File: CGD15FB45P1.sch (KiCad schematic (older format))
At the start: 9 parts, among them J12 CONN_02X13, U6 74LVC8T245, U7 74LVC2G04

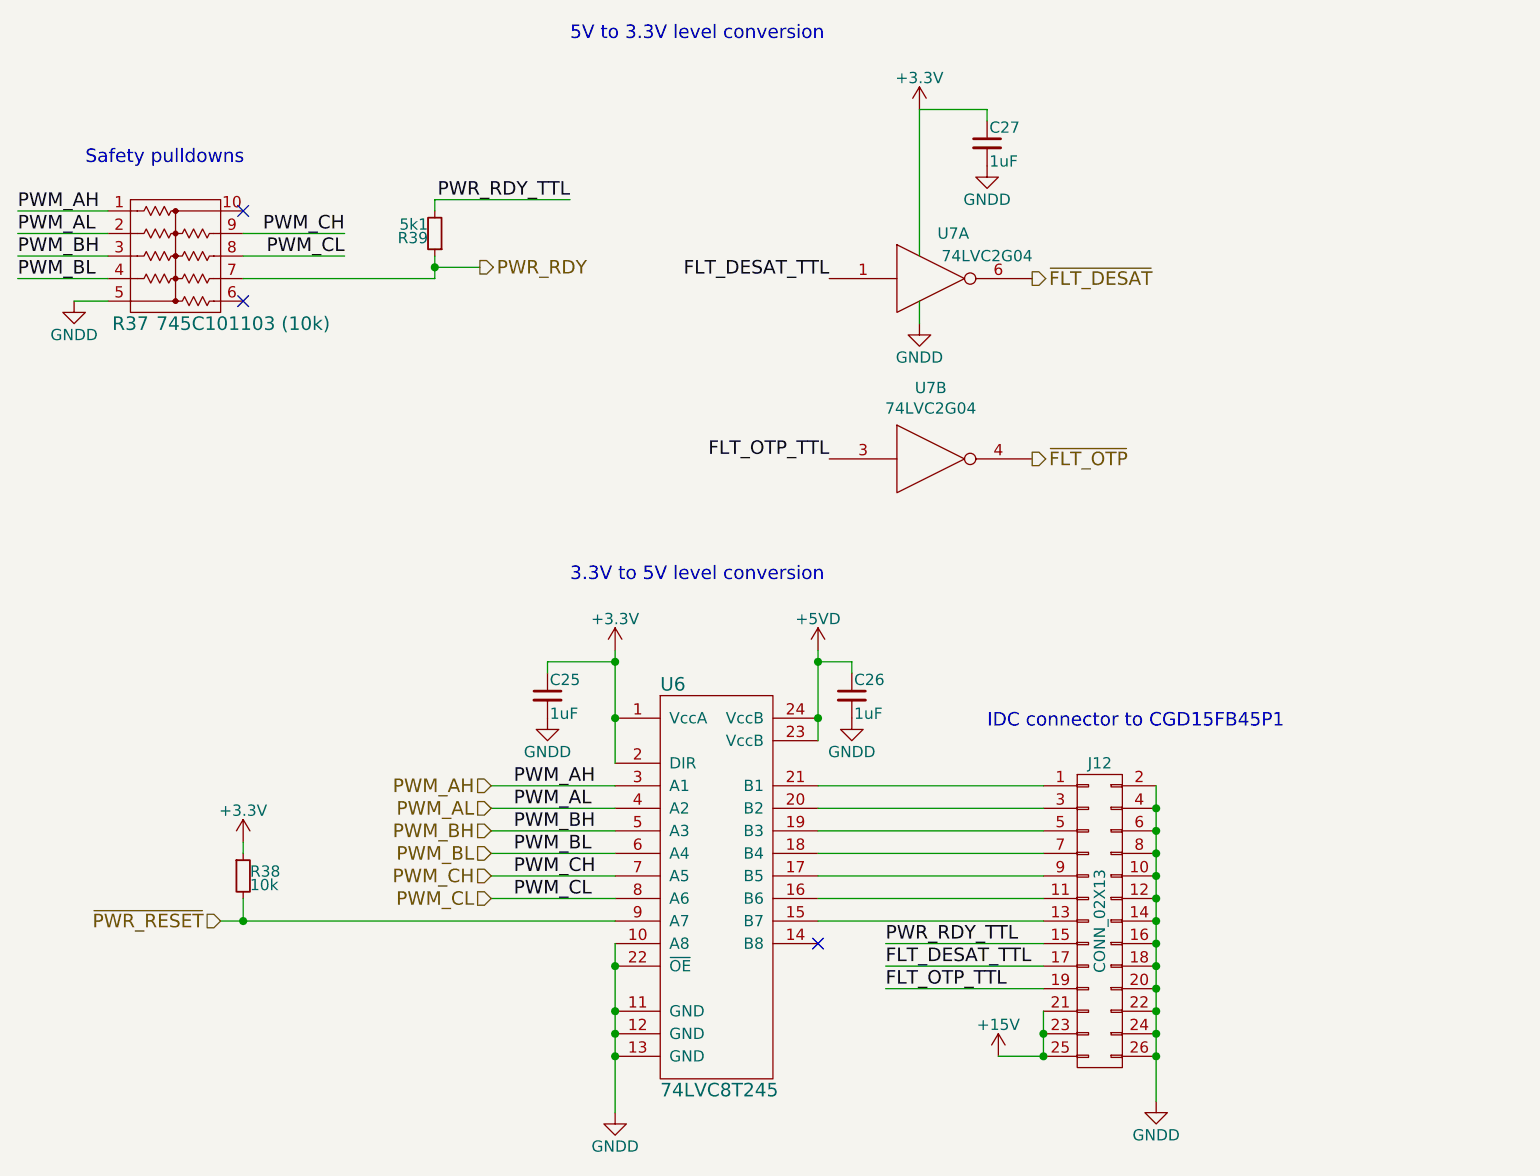
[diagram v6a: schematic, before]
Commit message: Swap level shifter pins for easier routing
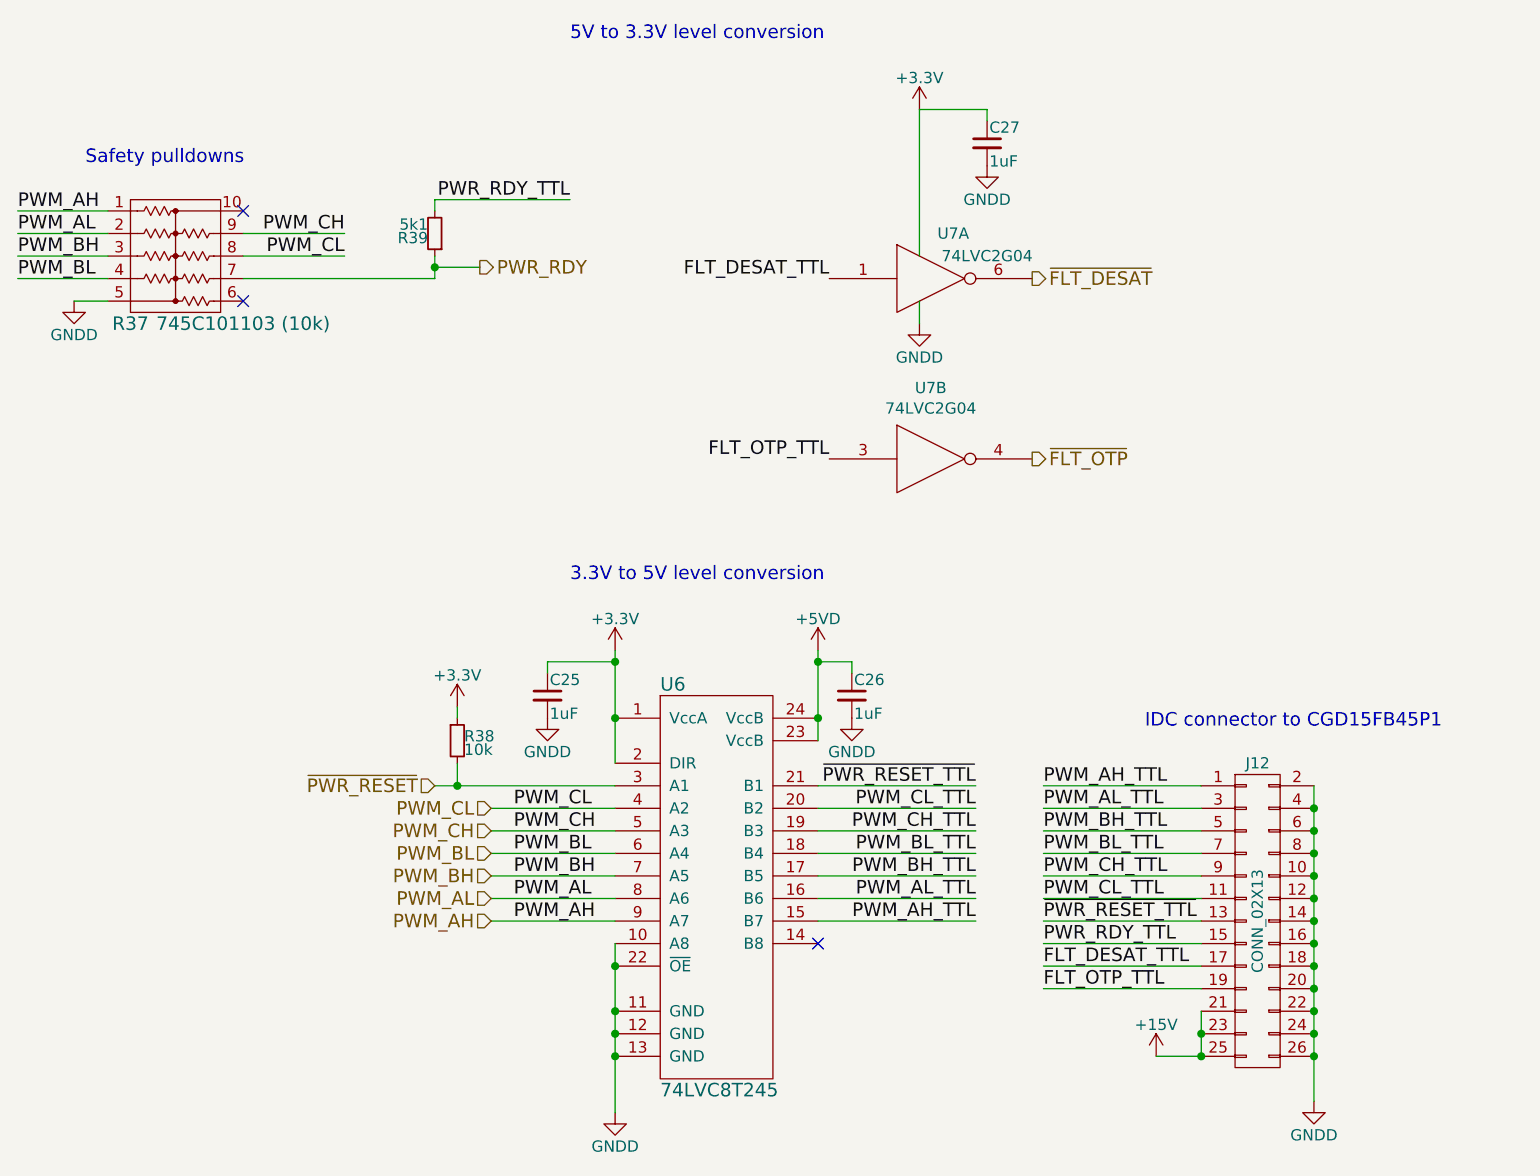
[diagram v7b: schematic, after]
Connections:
- net PWM_AH: now also U6.9 (A7); no longer U6.3 (A1)
- net PWM_AL: now also U6.8 (A6); no longer U6.4 (A2)
- net PWM_BH: now also U6.7 (A5); no longer U6.5 (A3)
- net PWM_CH: now also U6.5 (A3); no longer U6.7 (A5)
- net PWM_CL: now also U6.4 (A2); no longer U6.8 (A6)
- net ~PWR_RESET: now also U6.3 (A1); no longer U6.9 (A7)
- net PWM_AH_TTL: now reaches U6.15 (B7)
- net PWM_AH_TTL: now also J12.1 (P1); no longer J12.13 (P13)
- net PWM_AL_TTL: now reaches U6.16 (B6)
- net PWM_AL_TTL: now also J12.3 (P3); no longer J12.11 (P11)
- net PWM_BH_TTL: now reaches U6.17 (B5)
- net PWM_BH_TTL: now also J12.5 (P5); no longer J12.9 (P9)
- net PWM_BL_TTL: now reaches J12.7 (P7), U6.18 (B4)
- net PWM_CH_TTL: now reaches U6.19 (B3)
- net PWM_CH_TTL: now also J12.9 (P9); no longer J12.5 (P5)
- net PWM_CL_TTL: now reaches U6.20 (B2)
- net PWM_CL_TTL: now also J12.11 (P11); no longer J12.3 (P3)
- net ~PWR_RESET_TTL: now reaches U6.21 (B1)
- net ~PWR_RESET_TTL: now also J12.13 (P13); no longer J12.1 (P1)
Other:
- moved on the sheet: J12, R38
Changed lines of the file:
@@
 L GNDD #PWR071
 U 1 1 57A1908E
-P 7350 5850
-F 0 "#PWR071" H 7350 5600 50  0001 C CNN
-F 1 "GNDD" H 7350 5700 50  0000 C CNN
-F 2 "" H 7350 5850 50  0000 C CNN
-F 3 "" H 7350 5850 50  0000 C CNN
-	1    7350 5850
+P 8050 5850
+F 0 "#PWR071" H 8050 5600 50  0001 C CNN
+F 1 "GNDD" H 8050 5700 50  0000 C CNN
+F 2 "" H 8050 5850 50  0000 C CNN
+F 3 "" H 8050 5850 50  0000 C CNN
+	1    8050 5850
 	1    0    0    -1
 $EndComp
@@
 Text Label 4500 4750 0    60   ~ 0
 PWM_BL
-Text Label 4500 4850 0    60   ~ 0
+Text Label 4500 4650 0    60   ~ 0
 PWM_CH
-Text Label 4500 4950 0    60   ~ 0
+Text Label 4500 4550 0    60   ~ 0
 PWM_CL
-Text Label 6150 5250 0    60   ~ 0
+Text Label 6850 5250 0    60   ~ 0
 FLT_DESAT_TTL
 Text Label 3750 2100 2    60   ~ 0
@@
 L R_Small R38
 U 1 1 57A190B9
-P 3300 4850
-F 0 "R38" H 3330 4870 50  0000 L CNN
-F 1 "10k" H 3330 4810 50  0000 L CNN
-F 2 "Resistors_SMD:R_0603" H 3300 4850 50  0001 C CNN
-F 3 "" H 3300 4850 50  0000 C CNN
-	1    3300 4850
+P 4250 4250
+F 0 "R38" H 4280 4270 50  0000 L CNN
+F 1 "10k" H 4280 4210 50  0000 L CNN
+F 2 "Resistors_SMD:R_0603" H 4250 4250 50  0001 C CNN
+F 3 "" H 4250 4250 50  0000 C CNN
+	1    4250 4250
 	1    0    0    -1
 $EndComp
@@
 L CONN_02X13 J12
 U 1 1 57A190E8
-P 7100 5050
-F 0 "J12" H 7100 5750 50  0000 C CNN
-F 1 "CONN_02X13" V 7100 5050 50  0000 C CNN
-F 2 "Connect:IDC_Header_Straight_26pins" H 7100 3900 50  0001 C CNN
-F 3 "" H 7100 3900 50  0000 C CNN
-	1    7100 5050
-	1    0    0    -1
-$EndComp
-Text Label 4500 4450 0    60   ~ 0
+P 7800 5050
+F 0 "J12" H 7800 5750 50  0000 C CNN
+F 1 "CONN_02X13" V 7800 5050 50  0000 C CNN
+F 2 "Connect:IDC_Header_Straight_26pins" H 7800 3900 50  0001 C CNN
+F 3 "" H 7800 3900 50  0000 C CNN
+	1    7800 5050
+	1    0    0    -1
+$EndComp
+Text Label 4500 5050 0    60   ~ 0
 PWM_AH
-Text Label 4500 4550 0    60   ~ 0
+Text Label 4500 4950 0    60   ~ 0
 PWM_AL
-Text Label 4500 4650 0    60   ~ 0
+Text Label 4500 4850 0    60   ~ 0
 PWM_BH
 $Comp
 L +15V #PWR073
 U 1 1 57A190F2
-P 6650 5650
-F 0 "#PWR073" H 6650 5500 50  0001 C CNN
-F 1 "+15V" H 6650 5790 50  0000 C CNN
-F 2 "" H 6650 5650 50  0000 C CNN
-F 3 "" H 6650 5650 50  0000 C CNN
-	1    6650 5650
-	1    0    0    -1
-$EndComp
-Text Label 6150 5350 0    60   ~ 0
+P 7350 5650
+F 0 "#PWR073" H 7350 5500 50  0001 C CNN
+F 1 "+15V" H 7350 5790 50  0000 C CNN
+F 2 "" H 7350 5650 50  0000 C CNN
+F 3 "" H 7350 5650 50  0000 C CNN
+	1    7350 5650
+	1    0    0    -1
+$EndComp
+Text Label 6850 5350 0    60   ~ 0
 FLT_OTP_TTL
 $Comp
@@
 L +3.3V #PWR076
 U 1 1 57A19125
-P 3300 4700
-F 0 "#PWR076" H 3300 4550 50  0001 C CNN
-F 1 "+3.3V" H 3300 4840 50  0000 C CNN
-F 2 "" H 3300 4700 50  0000 C CNN
-F 3 "" H 3300 4700 50  0000 C CNN
-	1    3300 4700
+P 4250 4100
+F 0 "#PWR076" H 4250 3950 50  0001 C CNN
+F 1 "+3.3V" H 4250 4240 50  0000 C CNN
+F 2 "" H 4250 4100 50  0000 C CNN
+F 3 "" H 4250 4100 50  0000 C CNN
+	1    4250 4100
 	1    0    0    -1
 $EndComp
@@
 $EndComp
 Wire Wire Line
-	7350 4450 7350 5850
-Connection ~ 7350 4550
-Connection ~ 7350 4750
-Connection ~ 7350 4650
-Connection ~ 7350 4850
-Connection ~ 7350 4950
-Connection ~ 7350 5050
-Connection ~ 7350 5150
-Connection ~ 7350 5450
-Connection ~ 7350 5250
-Connection ~ 7350 5350
-Connection ~ 7350 5550
-Connection ~ 7350 5650
-Wire Wire Line
-	5850 4450 6850 4450
-Wire Wire Line
-	5850 4550 6850 4550
-Wire Wire Line
-	5850 4650 6850 4650
-Wire Wire Line
-	5850 4750 6850 4750
-Wire Wire Line
-	5850 4850 6850 4850
-Wire Wire Line
-	5850 4950 6850 4950
-Wire Wire Line
-	5850 5050 6850 5050
+	8050 4450 8050 5850
+Connection ~ 8050 4550
+Connection ~ 8050 4750
+Connection ~ 8050 4650
+Connection ~ 8050 4850
+Connection ~ 8050 4950
+Connection ~ 8050 5050
+Connection ~ 8050 5150
+Connection ~ 8050 5450
+Connection ~ 8050 5250
+Connection ~ 8050 5350
+Connection ~ 8050 5550
+Connection ~ 8050 5650
+Wire Wire Line
+	6850 4450 7550 4450
+Wire Wire Line
+	6850 4550 7550 4550
+Wire Wire Line
+	6850 4650 7550 4650
+Wire Wire Line
+	6850 4750 7550 4750
+Wire Wire Line
+	6850 4850 7550 4850
+Wire Wire Line
+	6850 4950 7550 4950
 Wire Wire Line
 	5850 3850 5850 4250
@@
 Connection ~ 4950 5250
 Wire Wire Line
-	4400 4450 4950 4450
+	4400 5050 4950 5050
+Wire Wire Line
+	4400 4950 4950 4950
+Wire Wire Line
+	4400 4850 4950 4850
+Wire Wire Line
+	4400 4750 4950 4750
+Wire Wire Line
+	4400 4650 4950 4650
 Wire Wire Line
 	4400 4550 4950 4550
-Wire Wire Line
-	4400 4650 4950 4650
-Wire Wire Line
-	4400 4750 4950 4750
-Wire Wire Line
-	4400 4850 4950 4850
-Wire Wire Line
-	4400 4950 4950 4950
 Connection ~ 5850 4150
 Wire Wire Line
-	6850 5450 6850 5650
-Wire Wire Line
-	6850 5650 6650 5650
-Wire Wire Line
-	6150 5150 6850 5150
-Wire Wire Line
-	6150 5250 6850 5250
-Wire Wire Line
-	6150 5350 6850 5350
+	7550 5450 7550 5650
+Wire Wire Line
+	7550 5650 7350 5650
+Wire Wire Line
+	6850 5150 7550 5150
+Wire Wire Line
+	6850 5250 7550 5250
+Wire Wire Line
+	6850 5350 7550 5350
 Connection ~ 4950 4150
 Wire Wire Line
@@
 	2550 2300 2700 2300
 Wire Wire Line
-	3300 4950 3300 5050
+	4250 4350 4250 4450
 Wire Wire Line
 	4150 1850 4750 1850
@@
 	1    0    0    -1
 $EndComp
-Text Label 6150 5150 0    60   ~ 0
+Text Label 6850 5150 0    60   ~ 0
 PWR_RDY_TTL
 Text HLabel 4350 2150 2    60   Output ~ 0
@@
 	1    0    0    -1
 $EndComp
-Connection ~ 6850 5550
-Connection ~ 6850 5650
+Connection ~ 7550 5550
+Connection ~ 7550 5650
 $Comp
 L GNDD #PWR079
@@
 Text Notes 4750 1150 0    60   ~ 0
 5V to 3.3V level conversion
-Text HLabel 3200 5050 0    60   Input ~ 0
+Text HLabel 4150 4450 0    60   Input ~ 0
 ~PWR_RESET
-Text HLabel 4400 4450 0    60   Input ~ 0
+Text HLabel 4400 5050 0    60   Input ~ 0
 PWM_AH
-Text HLabel 4400 4550 0    60   Input ~ 0
+Text HLabel 4400 4950 0    60   Input ~ 0
 PWM_AL
-Text HLabel 4400 4650 0    60   Input ~ 0
+Text HLabel 4400 4850 0    60   Input ~ 0
 PWM_BH
 Text HLabel 4400 4750 0    60   Input ~ 0
 PWM_BL
-Text HLabel 4400 4850 0    60   Input ~ 0
+Text HLabel 4400 4650 0    60   Input ~ 0
 PWM_CH
-Text HLabel 4400 4950 0    60   Input ~ 0
+Text HLabel 4400 4550 0    60   Input ~ 0
 PWM_CL
 Wire Wire Line
-	3200 5050 4950 5050
-Wire Wire Line
-	3300 4700 3300 4750
-Text Notes 6600 4200 0    60   ~ 0
+	4150 4450 4950 4450
+Wire Wire Line
+	4250 4100 4250 4150
+Text Notes 7300 4200 0    60   ~ 0
 IDC connector to CGD15FB45P1
 Text Notes 4750 3550 0    60   ~ 0
@@
 NoConn ~ 3300 1900
 NoConn ~ 5850 5150
-Connection ~ 3300 5050
+Connection ~ 4250 4450
+Text Label 6850 4450 0    60   ~ 0
+PWM_AH_TTL
+Text Label 6850 4550 0    60   ~ 0
+PWM_AL_TTL
+Text Label 6850 4650 0    60   ~ 0
+PWM_BH_TTL
+Text Label 6850 4750 0    60   ~ 0
+PWM_BL_TTL
+Text Label 6850 4850 0    60   ~ 0
+PWM_CH_TTL
+Text Label 6850 4950 0    60   ~ 0
+PWM_CL_TTL
+Wire Wire Line
+	6850 5050 7550 5050
+Text Label 6850 5050 0    60   ~ 0
+~PWR_RESET_TTL
+Wire Wire Line
+	6550 5050 5850 5050
+Wire Wire Line
+	6550 4950 5850 4950
+Wire Wire Line
+	6550 4850 5850 4850
+Wire Wire Line
+	6550 4750 5850 4750
+Wire Wire Line
+	6550 4650 5850 4650
+Wire Wire Line
+	6550 4550 5850 4550
+Text Label 6550 5050 2    60   ~ 0
+PWM_AH_TTL
+Text Label 6550 4950 2    60   ~ 0
+PWM_AL_TTL
+Text Label 6550 4850 2    60   ~ 0
+PWM_BH_TTL
+Text Label 6550 4750 2    60   ~ 0
+PWM_BL_TTL
+Text Label 6550 4650 2    60   ~ 0
+PWM_CH_TTL
+Text Label 6550 4550 2    60   ~ 0
+PWM_CL_TTL
+Text Label 6550 4450 2    60   ~ 0
+~PWR_RESET_TTL
+Wire Wire Line
+	5850 4450 6550 4450
 $EndSCHEMATC

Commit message: routing, but weird netnames on PWM
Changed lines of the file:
@@
 	1    0    0    -1
 $EndComp
-Text Label 4500 4750 0    60   ~ 0
-PWM_BL
-Text Label 4500 4650 0    60   ~ 0
-PWM_CH
+Text Label 4550 4750 0    60   ~ 0
+PWM_BL_
+Text Label 4550 4650 0    60   ~ 0
+PWM_CH_
 Text Label 4500 4550 0    60   ~ 0
 PWM_CL
@@
 $EndComp
 Wire Wire Line
-	8050 4450 8050 5850
+	8050 4450 8050 4550
+Wire Wire Line
+	8050 4550 8050 4650
+Wire Wire Line
+	8050 4650 8050 4750
+Wire Wire Line
+	8050 4750 8050 4850
+Wire Wire Line
+	8050 4850 8050 4950
+Wire Wire Line
+	8050 4950 8050 5050
+Wire Wire Line
+	8050 5050 8050 5150
+Wire Wire Line
+	8050 5150 8050 5250
+Wire Wire Line
+	8050 5250 8050 5350
+Wire Wire Line
+	8050 5350 8050 5450
+Wire Wire Line
+	8050 5450 8050 5550
+Wire Wire Line
+	8050 5550 8050 5650
+Wire Wire Line
+	8050 5650 8050 5850
 Connection ~ 8050 4550
 Connection ~ 8050 4750
@@
 	6850 4950 7550 4950
 Wire Wire Line
-	5850 3850 5850 4250
-Wire Wire Line
-	4950 5150 4950 5900
+	5850 3850 5850 3900
+Wire Wire Line
+	5850 3900 5850 4150
+Wire Wire Line
+	5850 4150 5850 4250
+Wire Wire Line
+	4950 5150 4950 5250
+Wire Wire Line
+	4950 5250 4950 5450
+Wire Wire Line
+	4950 5450 4950 5550
+Wire Wire Line
+	4950 5550 4950 5650
+Wire Wire Line
+	4950 5650 4950 5900
 Connection ~ 4950 5650
 Connection ~ 4950 5550
 Wire Wire Line
-	4950 3850 4950 4350
+	4950 3850 4950 3900
+Wire Wire Line
+	4950 3900 4950 4150
+Wire Wire Line
+	4950 4150 4950 4350
 Connection ~ 4950 5450
 Connection ~ 4950 5250
@@
 Connection ~ 5850 4150
 Wire Wire Line
-	7550 5450 7550 5650
+	7550 5450 7550 5550
+Wire Wire Line
+	7550 5550 7550 5650
 Wire Wire Line
 	7550 5650 7350 5650
@@
 	4150 1850 4150 1900
 Wire Wire Line
-	4150 2100 4150 2200
+	4150 2100 4150 2150
+Wire Wire Line
+	4150 2150 4150 2200
 Wire Wire Line
 	4350 2150 4150 2150
@@
 PWM_CL
 Wire Wire Line
-	4150 4450 4950 4450
+	4150 4450 4250 4450
+Wire Wire Line
+	4250 4450 4950 4450
 Wire Wire Line
 	4250 4100 4250 4150
